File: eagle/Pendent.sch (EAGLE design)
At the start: 40 parts, among them Q1 CMA-4544PF-W, Q2 MPSA42, Q3 8/16/20MHz, U1 MAX9814TDFN14, U2 LF50ABDT-TR, U3 ATMEGA328

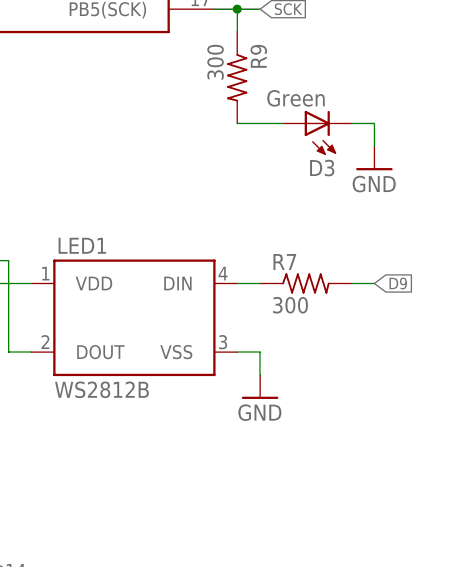
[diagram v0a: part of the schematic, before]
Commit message: Wire up Sleep Button
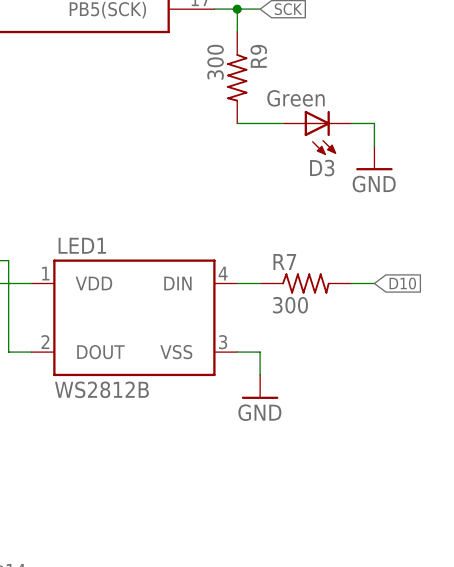
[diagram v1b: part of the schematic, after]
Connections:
- net D10: now also R7.2
- net D9: no longer R7.2
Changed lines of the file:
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@@
-</segment>
-<segment>
-<pinref part="R7" gate="G$1" pin="2"/>
-<wire x1="144.78" y1="116.84" x2="147.32" y2="116.84" width="0.1524" layer="91"/>
-<label x="147.32" y="116.84" size="1.27" layer="95" xref="yes"/>
 </segment>
 <segment>
@@
 <label x="132.08" y="154.94" size="1.27" layer="95" xref="yes"/>
 </segment>
+<segment>
+<pinref part="R7" gate="G$1" pin="2"/>
+<wire x1="144.78" y1="116.84" x2="147.32" y2="116.84" width="0.1524" layer="91"/>
+<label x="147.32" y="116.84" size="1.27" layer="95" xref="yes"/>
+</segment>
 </net>

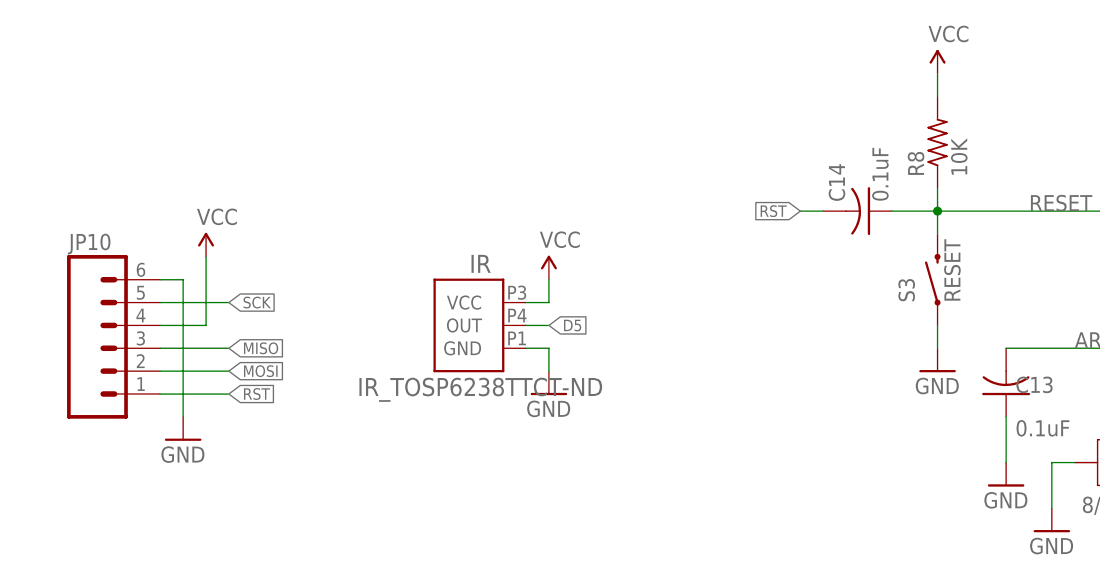
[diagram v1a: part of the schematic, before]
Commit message: Add Bigger Tempo Button to board
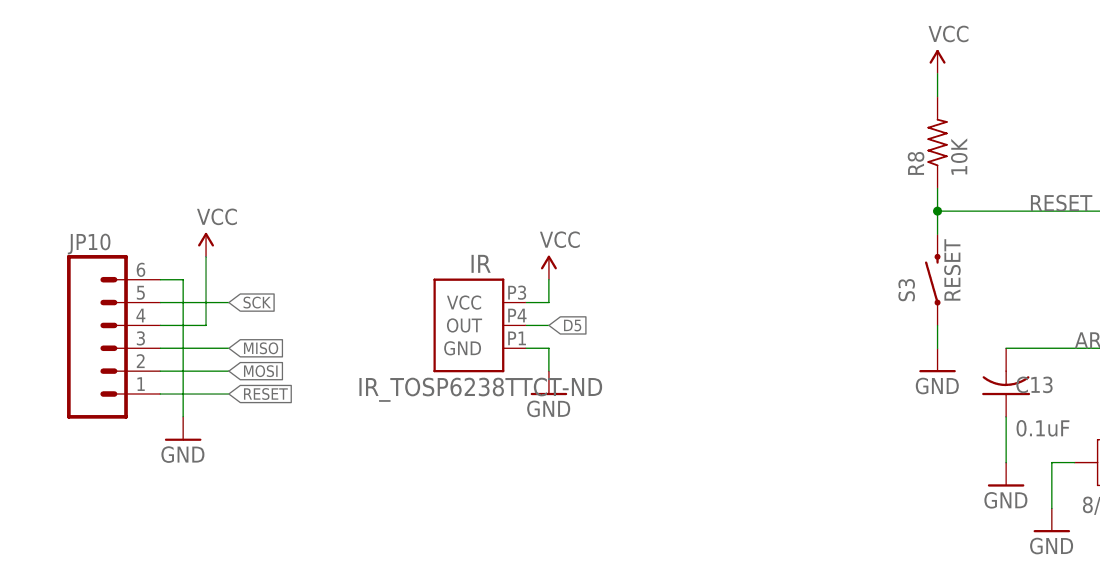
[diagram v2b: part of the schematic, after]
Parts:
- removed C14: 0.1uF, adafruit:C-USC0805K
- S1: device SparkFun-Electromechanical:SWITCH-MOMENTARY-2SMD-REDUNDANT -> bg_eagle_lib:SWITCH-PUSHBUTTON
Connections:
- removed net RST: C14.2, JP10.1
- net RESET: now also JP10.1; no longer C14.1
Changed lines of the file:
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@@
 <part name="P+1" library="SparkFun" deviceset="VCC" device=""/>
 <part name="GND10" library="supply1" deviceset="GND" device=""/>
-<part name="S1" library="SparkFun-Electromechanical" deviceset="SWITCH-MOMENTARY-2" device="SMD-REDUNDANT" value="Tempo"/>
+<part name="S1" library="bg_eagle_lib" deviceset="SWITCH-PUSHBUTTON" device="" value="Tempo"/>
 <part name="GND11" library="SparkFun" deviceset="GND" device=""/>
 <part name="Q2" library="SparkFun-DiscreteSemi" deviceset="TRANSISTOR_NPN" device="MPSA42" value="MPSA42"/>
@@
 <part name="P+10" library="SparkFun" deviceset="3.3V" device="" value="VCC"/>
 <part name="GND21" library="SparkFun" deviceset="GND" device=""/>
-<part name="C14" library="adafruit" deviceset="C-US" device="C0805K" value="0.1uF"/>
 <part name="S3" library="Testing" deviceset="SWITCH-MOMENTARY-2" device="SMD-ALT01" value="RESET"/>
 <part name="Q3" library="Testing" deviceset="RESONATOR" device="1:1" value="8/16/20MHz"/>
@@
 <instance part="P+10" gate="G$1" x="78.74" y="208.28"/>
 <instance part="GND21" gate="1" x="78.74" y="144.78"/>
-<instance part="C14" gate="G$1" x="48.26" y="205.74" smashed="yes" rot="R270">
-<attribute name="NAME" x="45.593" y="206.756" size="1.778" layer="95" rot="R90"/>
-<attribute name="VALUE" x="50.419" y="206.756" size="1.778" layer="96" rot="R90"/>
-</instance>
 <instance part="S3" gate="G$1" x="55.88" y="198.12" rot="R90"/>
 <instance part="Q3" gate="G$1" x="78.74" y="177.8" smashed="yes" rot="R270">
@@
 </segment>
 </net>
-<net name="RST" class="0">
-<segment>
-<label x="-22.86" y="185.42" size="1.27" layer="95" xref="yes"/>
-<pinref part="JP10" gate="G$1" pin="1"/>
-<wire x1="-22.86" y1="185.42" x2="-30.48" y2="185.42" width="0.1524" layer="91"/>
-</segment>
-<segment>
-<pinref part="C14" gate="G$1" pin="2"/>
-<wire x1="43.18" y1="205.74" x2="40.64" y2="205.74" width="0.1524" layer="91"/>
-<label x="40.64" y="205.74" size="1.27" layer="95" rot="R180" xref="yes"/>
-</segment>
-</net>
 <net name="N$22" class="0">
 <segment>
@@
 <wire x1="55.88" y1="208.28" x2="55.88" y2="205.74" width="0.1524" layer="91"/>
 <wire x1="55.88" y1="203.2" x2="55.88" y2="205.74" width="0.1524" layer="91"/>
-<wire x1="55.88" y1="205.74" x2="50.8" y2="205.74" width="0.1524" layer="91"/>
 <junction x="55.88" y="205.74"/>
 <label x="66.04" y="205.74" size="1.778" layer="95"/>
 <pinref part="U3" gate="G$1" pin="PC6(/RESET)"/>
 <pinref part="R8" gate="G$1" pin="1"/>
-<pinref part="C14" gate="G$1" pin="1"/>
 <pinref part="S3" gate="G$1" pin="2"/>
 </segment>
-</net>
+<segment>
+<pinref part="JP10" gate="G$1" pin="1"/>
+<wire x1="-30.48" y1="185.42" x2="-22.86" y2="185.42" width="0.1524" layer="91"/>
+<label x="-22.86" y="185.42" size="1.27" layer="95" xref="yes"/>
+</segment>
+</net>
